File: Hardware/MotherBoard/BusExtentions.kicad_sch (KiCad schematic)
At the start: 10 parts, among them J3 ISA00, J4 ISA10, J7 ISA01, J8 ISA11, U10 74HCT541, U11 SN74LVC245AN, U12 SN74LVC245AN, U13 74HCT541, U14 74HCT541, U9 74HCT541

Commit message: Fix
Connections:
- no-connect marks 1 -> 3
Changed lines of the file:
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@@
 (kicad_sch (version 20201015) (generator eeschema)
-  (page 1 4)
+  (page 1 1)
   (paper "A4")
   (junction (at 63.5 100.33) (diameter 1.016) (color 0 0 0 0))
@@
   (junction (at 165.1 99.06) (diameter 1.016) (color 0 0 0 0))
   (no_connect (at 170.815 65.405))
+  (no_connect (at 72.39 156.845))
+  (no_connect (at 156.21 155.575))
   (bus_entry (at 114.935 34.925) (size 2.54 2.54)
     (stroke (width 0.1524) (type solid) (color 0 0 0 0))
@@
     )
   )
+  (sheet_instances
+    (path "/" (page "1"))
+  )
+  (symbol_instances
+    (path "/aae262a5-980b-4be4-a85e-c2cf7b799405"
+      (reference "#PWR0125") (unit 1) (value "GND") (footprint "")
+    )
+    (path "/6a470757-4358-44cd-82a5-db2d64fa6f54"
+      (reference "#PWR0126") (unit 1) (value "+5V") (footprint "")
+    )
+    (path "/8ce2b343-39c5-4211-9032-d8a415207f99"
+      (reference "#PWR0127") (unit 1) (value "+5V") (footprint "")
+    )
+    (path "/a4357a5a-e4dd-4f1a-80a8-1ac3bdfec736"
+      (reference "#PWR0128") (unit 1) (value "+5V") (footprint "")
+    )
+    (path "/be3c90d2-460f-475a-b8d5-c0fa479568d2"
+      (reference "#PWR0129") (unit 1) (value "GND") (footprint "")
+    )
+    (path "/f15ea47b-eb16-4e14-b8e7-e5d42077b88a"
+      (reference "#PWR0130") (unit 1) (value "GND") (footprint "")
+    )
+    (path "/a9ee1bb1-999b-4256-98ad-699c35645a30"
+      (reference "#PWR0131") (unit 1) (value "GND") (footprint "")
+    )
+    (path "/590f7ac6-3605-40fb-97be-8ffdd6cd7ecd"
+      (reference "#PWR0132") (unit 1) (value "+5V") (footprint "")
+    )
+    (path "/a33e05e8-4a0b-4de9-82f3-216a64ed2403"
+      (reference "J3") (unit 1) (value "ISA00") (footprint "Connector_PinSocket_2.54mm:PinSocket_1x15_P2.54mm_Vertical")
+    )
+    (path "/ad97b31a-c5ce-4faa-a2d0-e001fa0cc350"
+      (reference "J4") (unit 1) (value "ISA10") (footprint "Connector_PinSocket_2.54mm:PinSocket_1x15_P2.54mm_Vertical")
+    )
+    (path "/fa838b97-f421-46fa-ac1e-9a2f6ddd7e0c"
+      (reference "J7") (unit 1) (value "ISA01") (footprint "Connector_PinSocket_2.54mm:PinSocket_1x15_P2.54mm_Vertical")
+    )
+    (path "/19cc7f8e-7a0d-4fe2-9625-721aeb7bd93d"
+      (reference "J8") (unit 1) (value "ISA11") (footprint "Connector_PinSocket_2.54mm:PinSocket_1x15_P2.54mm_Vertical")
+    )
+    (path "/1e640dc0-9a9b-4e78-97a7-c4c4fba75621"
+      (reference "U9") (unit 1) (value "74HCT541") (footprint "Package_DIP:DIP-20_W7.62mm")
+    )
+    (path "/87eea902-e28a-40ef-a5ce-0c008a75322f"
+      (reference "U10") (unit 1) (value "74HCT541") (footprint "Package_DIP:DIP-20_W7.62mm")
+    )
+    (path "/e8617ace-d039-40cf-88f5-54844f714e69"
+      (reference "U11") (unit 1) (value "SN74LVC245AN") (footprint "Package_DIP:DIP-20_W7.62mm")
+    )
+    (path "/3cca239b-f779-41bf-b799-10b7e05ec0c1"
+      (reference "U12") (unit 1) (value "SN74LVC245AN") (footprint "Package_DIP:DIP-20_W7.62mm")
+    )
+    (path "/307f46a0-ac22-48e0-8f31-60c6b44a6ba9"
+      (reference "U13") (unit 1) (value "74HCT541") (footprint "Package_DIP:DIP-20_W7.62mm")
+    )
+    (path "/a0cfc135-bc69-4e94-b73e-3f2d947b9990"
+      (reference "U14") (unit 1) (value "74HCT541") (footprint "Package_DIP:DIP-20_W7.62mm")
+    )
+  )

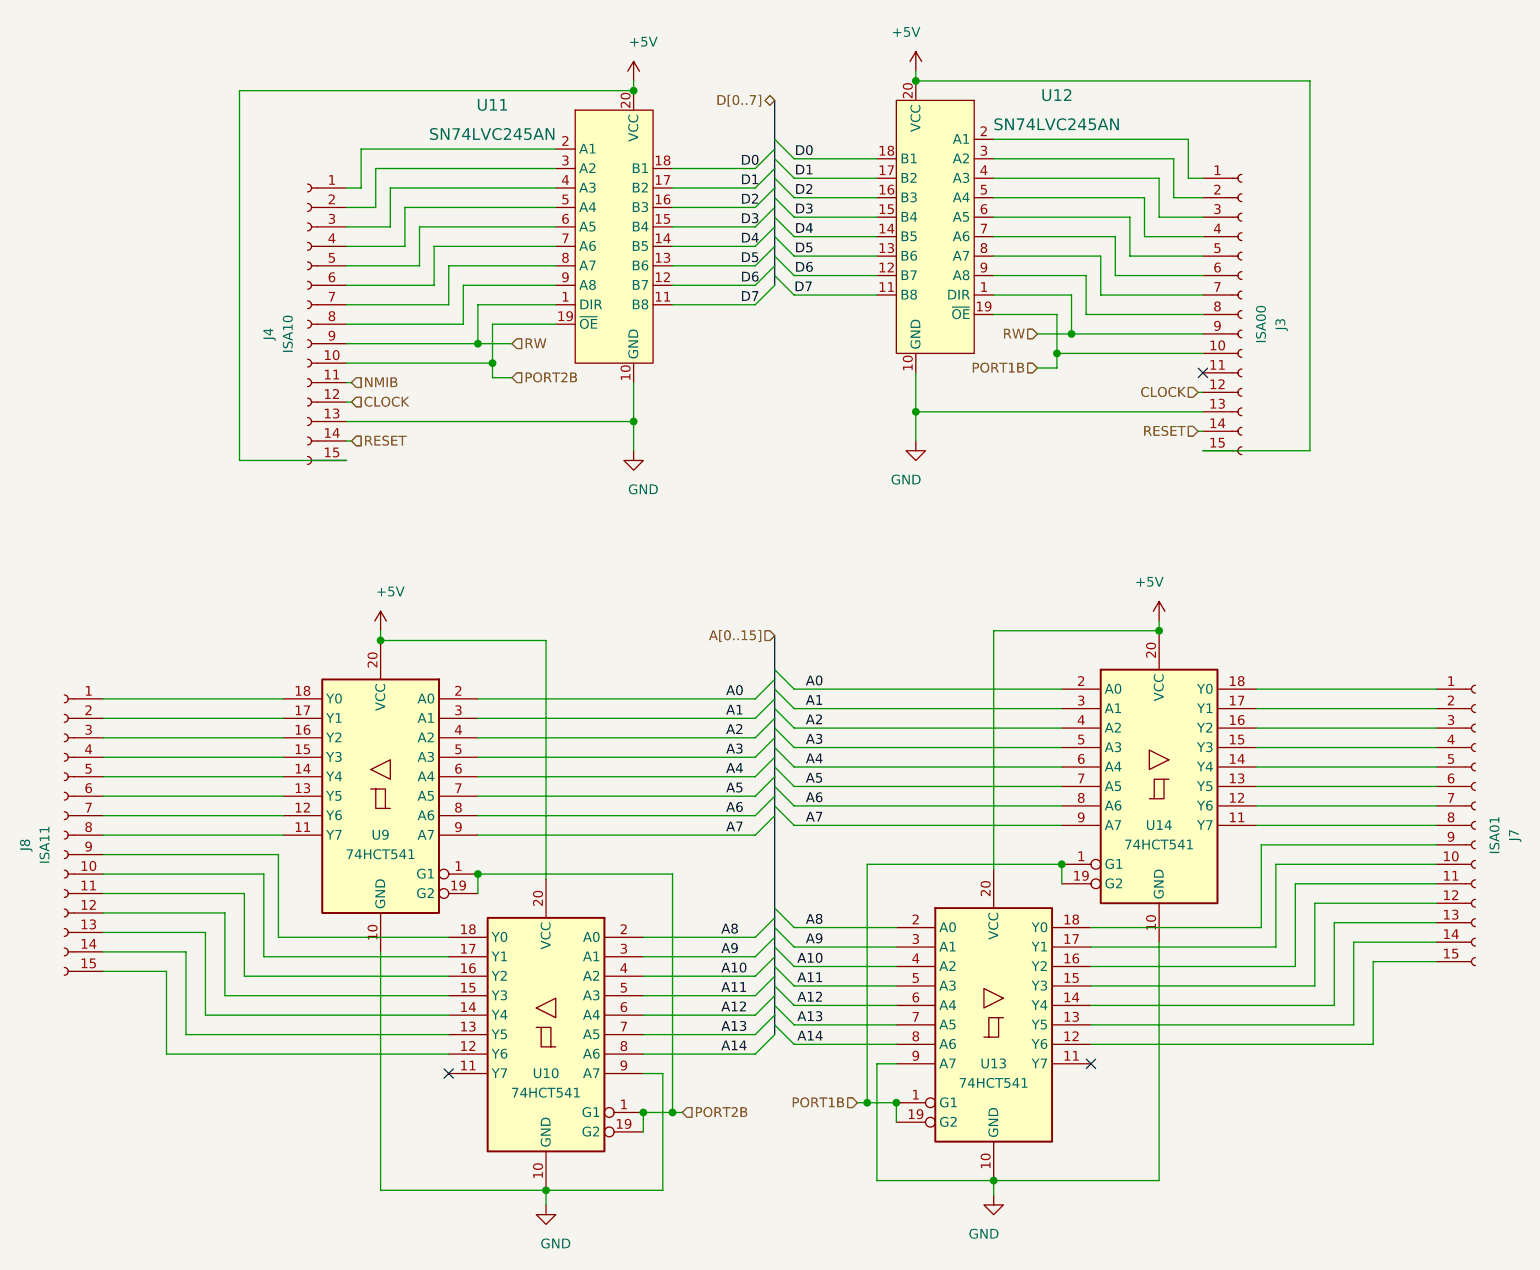
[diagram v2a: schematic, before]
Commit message: Replace logic IC 4xxx by 74hcxx
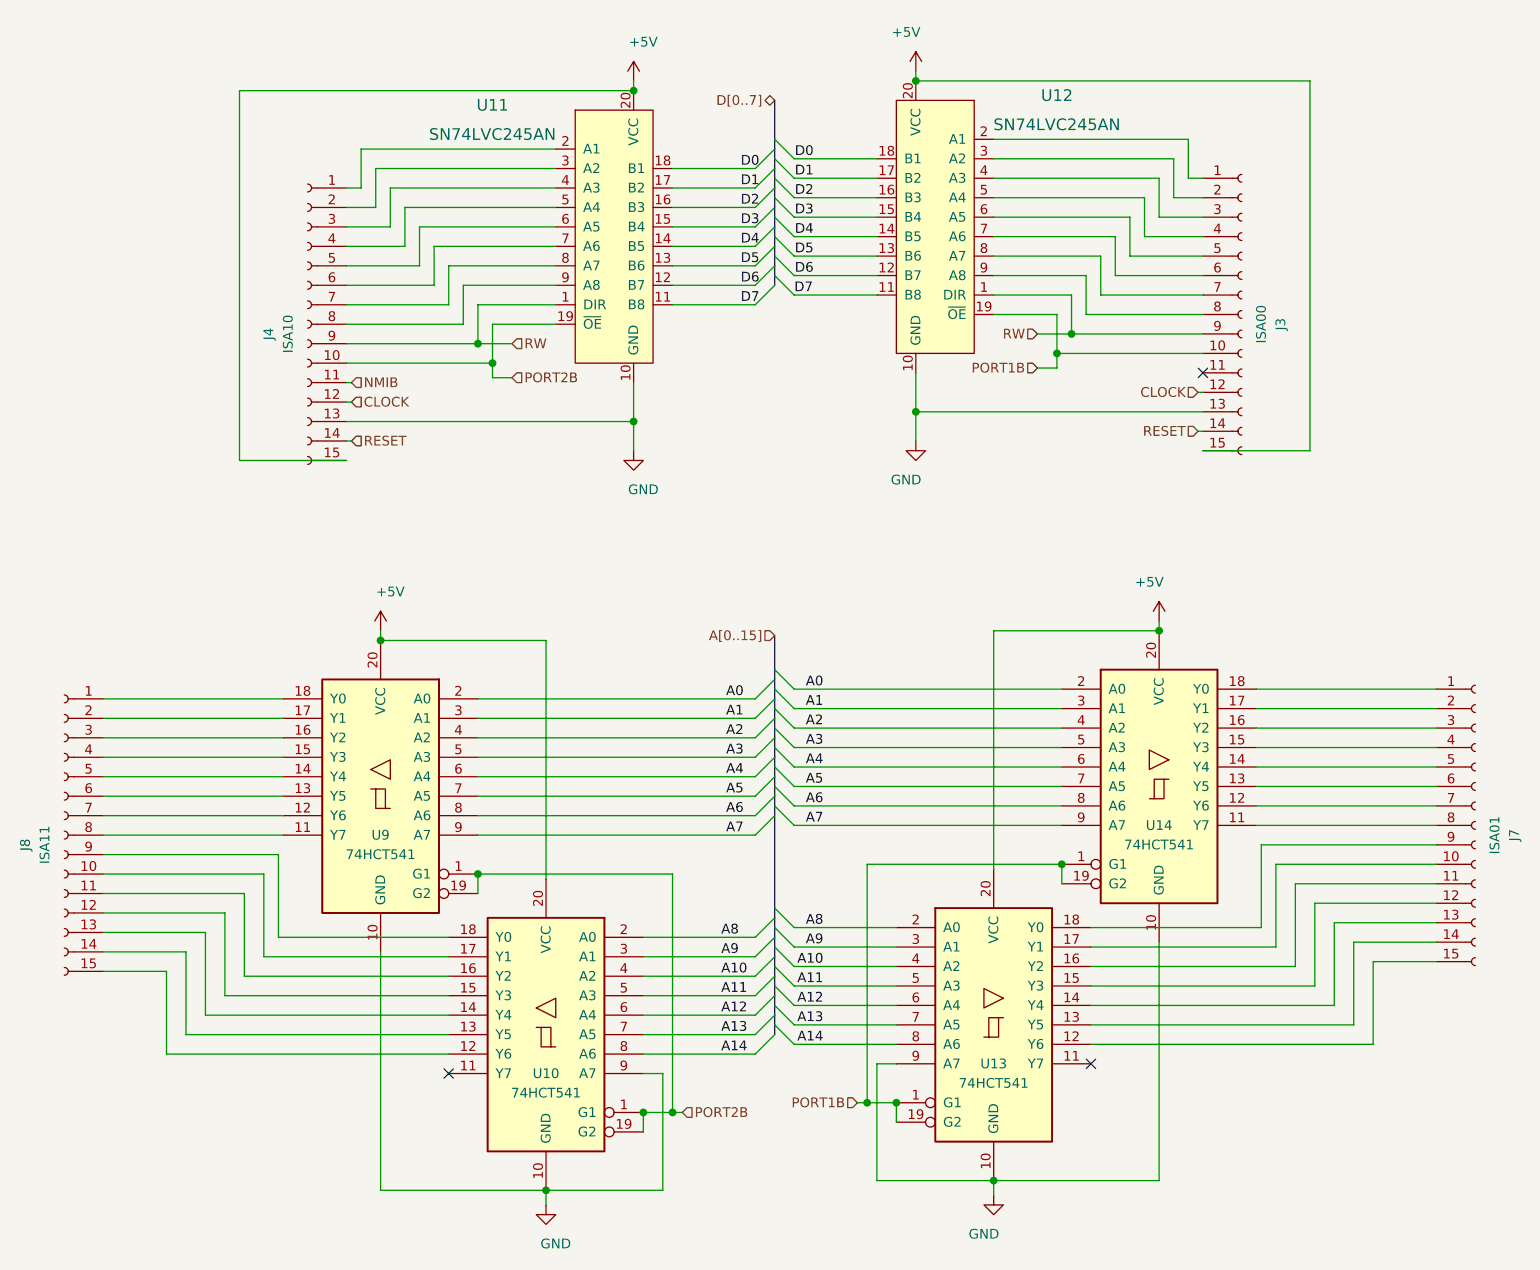
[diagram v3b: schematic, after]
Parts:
- U11, U12: footprint Package_DIP:DIP-20_W7.62mm -> digikey-footprints:DIP-20_W7.62mm
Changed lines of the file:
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@@
   (junction (at 165.1 99.06) (diameter 1.016) (color 0 0 0 0))
   (no_connect (at 170.815 65.405))
+  (no_connect (at 72.39 156.845))
   (no_connect (at 156.21 155.575))
-  (no_connect (at 72.39 156.845))
   (bus_entry (at 114.935 34.925) (size 2.54 2.54)
     (stroke (width 0.1524) (type solid) (color 0 0 0 0))
@@
     )
   )
-  (symbol (lib_id "Connector:Conn_01x15_Female") (at 53.975 59.055 0) (mirror y) (unit 1)
+  (symbol (lib_name "Connector:Conn_01x15_Female_2") (lib_id "Connector:Conn_01x15_Female") (at 53.975 59.055 0) (mirror y) (unit 1)
     (in_bom yes) (on_board yes)
     (property "Reference" "J4" (id 0) (at 48.895 60.325 90))
@@
     )
   )
-  (symbol (lib_id "Connector:Conn_01x15_Female") (at 175.895 57.785 0) (unit 1)
+  (symbol (lib_name "Connector:Conn_01x15_Female_1") (lib_id "Connector:Conn_01x15_Female") (at 175.895 57.785 0) (unit 1)
     (in_bom yes) (on_board yes)
     (property "Reference" "J3" (id 0) (at 180.975 59.055 90))
@@
     )
   )
-  (symbol (lib_id "Connector:Conn_01x15_Female") (at 206.375 124.46 0) (unit 1)
+  (symbol (lib_name "Connector:Conn_01x15_Female_3") (lib_id "Connector:Conn_01x15_Female") (at 206.375 124.46 0) (unit 1)
     (in_bom yes) (on_board yes)
     (property "Reference" "J7" (id 0) (at 211.455 125.73 90))
@@
     )
   )
-  (symbol (lib_id "dk_Logic-Buffers-Drivers-Receivers-Transceivers:SN74LVC245AN") (at 96.52 36.195 0) (unit 1)
+  (symbol (lib_name "dk_Logic-Buffers-Drivers-Receivers-Transceivers:SN74LVC245AN_1") (lib_id "dk_Logic-Buffers-Drivers-Receivers-Transceivers:SN74LVC245AN") (at 96.52 36.195 0) (unit 1)
     (in_bom yes) (on_board yes)
     (property "Reference" "U11" (id 0) (at 78.105 30.48 0)
@@
       (effects (font (size 1.524 1.524)))
     )
-    (property "Footprint" "Package_DIP:DIP-20_W7.62mm" (id 2) (at 101.6 31.115 0)
+    (property "Footprint" "digikey-footprints:DIP-20_W7.62mm" (id 2) (at 101.6 31.115 0)
       (effects (font (size 1.524 1.524)) (justify left) hide)
     )
@@
       (effects (font (size 1.524 1.524)))
     )
-    (property "Footprint" "Package_DIP:DIP-20_W7.62mm" (id 2) (at 128.27 29.845 0)
+    (property "Footprint" "digikey-footprints:DIP-20_W7.62mm" (id 2) (at 128.27 29.845 0)
       (effects (font (size 1.524 1.524)) (justify left) hide)
     )
@@
     )
   )
-  (symbol (lib_id "74xx:74HCT541") (at 63.5 120.65 0) (mirror y) (unit 1)
+  (symbol (lib_name "74xx:74HCT541_1") (lib_id "74xx:74HCT541") (at 63.5 120.65 0) (mirror y) (unit 1)
     (in_bom yes) (on_board yes)
     (property "Reference" "U9" (id 0) (at 63.5 125.73 0))
@@
     )
   )
-  (symbol (lib_id "74xx:74HCT541") (at 143.51 150.495 0) (unit 1)
+  (symbol (lib_name "74xx:74HCT541_3") (lib_id "74xx:74HCT541") (at 143.51 150.495 0) (unit 1)
     (in_bom yes) (on_board yes)
     (property "Reference" "U13" (id 0) (at 143.51 155.575 0))
@@
     )
   )
-  (symbol (lib_id "74xx:74HCT541") (at 165.1 119.38 0) (unit 1)
+  (symbol (lib_name "74xx:74HCT541_2") (lib_id "74xx:74HCT541") (at 165.1 119.38 0) (unit 1)
     (in_bom yes) (on_board yes)
     (property "Reference" "U14" (id 0) (at 165.1 124.46 0))

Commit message: Finalize daughter board
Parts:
- U11, U12: footprint digikey-footprints:DIP-20_W7.62mm -> Package_DIP:DIP-20_W7.62mm
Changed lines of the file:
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@@
 (kicad_sch (version 20201015) (generator eeschema)
-  (page 1 4)
   (paper "A4")
   (junction (at 63.5 100.33) (diameter 1.016) (color 0 0 0 0))
@@
   (junction (at 153.67 60.325) (diameter 1.016) (color 0 0 0 0))
   (junction (at 165.1 99.06) (diameter 1.016) (color 0 0 0 0))
+  (no_connect (at 156.21 155.575))
   (no_connect (at 170.815 65.405))
   (no_connect (at 72.39 156.845))
-  (no_connect (at 156.21 155.575))
   (bus_entry (at 114.935 34.925) (size 2.54 2.54)
     (stroke (width 0.1524) (type solid) (color 0 0 0 0))
@@
       (effects (font (size 1.524 1.524)))
     )
-    (property "Footprint" "digikey-footprints:DIP-20_W7.62mm" (id 2) (at 101.6 31.115 0)
+    (property "Footprint" "Package_DIP:DIP-20_W7.62mm" (id 2) (at 101.6 31.115 0)
       (effects (font (size 1.524 1.524)) (justify left) hide)
     )
@@
       (effects (font (size 1.524 1.524)))
     )
-    (property "Footprint" "digikey-footprints:DIP-20_W7.62mm" (id 2) (at 128.27 29.845 0)
+    (property "Footprint" "Package_DIP:DIP-20_W7.62mm" (id 2) (at 128.27 29.845 0)
       (effects (font (size 1.524 1.524)) (justify left) hide)
     )
